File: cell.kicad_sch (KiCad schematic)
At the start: 31 parts, among them K4 V23105A5001A201, Q12 IRLML0030, Q13 IRLML0030, SW8 SW_SPST, SW9 SW_SPST, U6 LMV324

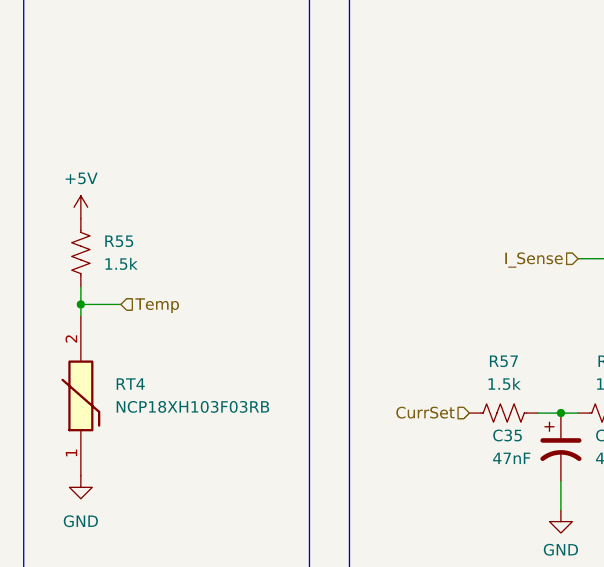
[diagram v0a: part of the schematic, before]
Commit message: Updated the ADC, whoopsies
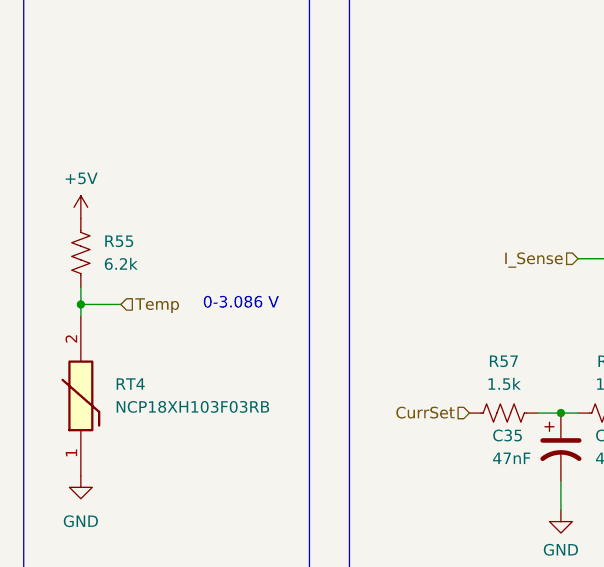
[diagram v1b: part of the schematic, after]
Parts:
- R55: value 1.5k -> 6.2k
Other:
- note added: "0-3.086 V"
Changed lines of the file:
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@@
 		)
 	)
+	(text "0-3.086 V"
+		(exclude_from_sim no)
+		(at 132.08 75.565 0)
+		(effects
+			(font
+				(size 1.27 1.27)
+			)
+		)
+	)
 	(text "CURRENT CONTROL"
 		(exclude_from_sim no)
@@
 			)
 		)
-		(property "Value" "1.5k"
+		(property "Value" "6.2k"
 			(at 116.84 71.1199 0)
 			(effects
